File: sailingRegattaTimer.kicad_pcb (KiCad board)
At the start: 2 copper layers, 58 x 68 mm, 29 parts, among them J1 Power, J1-Red-1M1 Conn_01x02_Socket, J2 Digital/PWM, J2-Yel-2M1 Conn_01x02_Socket, J3 Analog, J3-Grn-3M1 J3-Grn-3M, J4 Digital/PWM, J4-Blu-5M1 J4-Blu-5M1, J5-5v-LED1 Conn_01x02_Socket, J6-Reset1 J6-Reset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

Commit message: incremental save
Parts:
- moved D1-LED 0.56 mm to (135.2, 68.6)
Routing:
- net GND: track 165.0 -> 155.5 mm
- net +5V: track 169.1 -> 170.1 mm
- net /4: track 56.0 -> 55.5 mm

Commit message: update files, prep for PCB Way contact
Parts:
- moved D1-LED 0.50 mm to (135.2, 69.1)
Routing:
- net GND: track 155.5 -> 173.5 mm
- net /4: track 55.5 -> 56.0 mm

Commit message: commit to save interim work
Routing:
- net GND: track 173.5 -> 171.3 mm
- net +5V: track 170.1 -> 168.3 mm
- net /4: track 56.0 -> 55.0 mm
- net /2: track 30.2 -> 29.3 mm
- net Net-(D1-K): track 37.0 -> 36.5 mm
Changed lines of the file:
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@@
 	)
 	(segment
-		(start 127 78)
-		(end 127.5 77.5)
+		(start 135 55.25)
+		(end 132 52.25)
 		(width 0.25)
 		(layer "F.Cu")
@@
 	)
 	(segment
-		(start 134.05 60)
-		(end 134 59.95)
-		(width 0.25)
-		(layer "F.Cu")
-		(net 1)
-	)
-	(segment
 		(start 138.75 81.75)
 		(end 138.75 88.75)
@@
 	)
 	(segment
+		(start 135 60.75)
+		(end 135 55.25)
+		(width 0.25)
+		(layer "F.Cu")
+		(net 1)
+	)
+	(segment
 		(start 155.995 92)
 		(end 155.995 94.495)
@@
 	)
 	(segment
-		(start 134 59.95)
-		(end 134 51.75)
+		(start 132 52.25)
+		(end 129.466 52.25)
 		(width 0.25)
 		(layer "F.Cu")
@@
 	)
 	(segment
-		(start 134 51.75)
-		(end 128.966 51.75)
-		(width 0.25)
-		(layer "F.Cu")
-		(net 1)
-	)
-	(segment
 		(start 155.995 70.5)
 		(end 155.995 60.505)
@@
 	)
 	(segment
-		(start 133.3 60.75)
-		(end 134.05 60)
-		(width 0.25)
-		(layer "F.Cu")
-		(net 1)
-	)
-	(segment
-		(start 128.966 51.75)
-		(end 126.416 49.2)
-		(width 0.25)
-		(layer "F.Cu")
-		(net 1)
-	)
-	(segment
-		(start 155.995 60.505)
-		(end 156.5 60)
-		(width 0.25)
-		(layer "F.Cu")
-		(net 1)
-	)
-	(segment
 		(start 145.89 94.75)
 		(end 143.18 97.46)
@@
 	)
 	(segment
+		(start 133.3 60.75)
+		(end 135 60.75)
+		(width 0.25)
+		(layer "F.Cu")
+		(net 1)
+	)
+	(segment
 		(start 155.995 94.495)
 		(end 155.74 94.75)
@@
 	)
 	(segment
-		(start 123.04 88.71)
-		(end 122.5 88.71)
+		(start 129.466 52.25)
+		(end 126.416 49.2)
 		(width 0.25)
 		(layer "F.Cu")
@@
 	)
 	(segment
-		(start 138.25 95.07)
-		(end 140.64 97.46)
+		(start 138.5 94)
+		(end 136 91.5)
+		(width 0.25)
+		(layer "B.Cu")
+		(net 1)
+	)
+	(segment
+		(start 140.64 97.46)
+		(end 140.64 95.14)
+		(width 0.25)
+		(layer "B.Cu")
+		(net 1)
+	)
+	(segment
+		(start 139.5 94)
+		(end 138.5 94)
+		(width 0.25)
+		(layer "B.Cu")
+		(net 1)
+	)
+	(segment
+		(start 140.64 95.14)
+		(end 139.5 94)
 		(width 0.25)
 		(layer "B.Cu")
@@
 	)
 	(segment
-		(start 138.25 91.75)
-		(end 138.25 95.07)
-		(width 0.25)
-		(layer "B.Cu")
-		(net 1)
-	)
-	(segment
 		(start 121.75 68)
 		(end 126.05 68)
@@
 	)
 	(segment
-		(start 136 91.5)
-		(end 138 91.5)
-		(width 0.25)
-		(layer "B.Cu")
-		(net 1)
-	)
-	(segment
 		(start 126.05 68)
 		(end 133.3 60.75)
@@
 	)
 	(segment
-		(start 138 91.5)
-		(end 138.25 91.75)
-		(width 0.25)
-		(layer "B.Cu")
-		(net 1)
-	)
-	(segment
 		(start 133.3 58.55)
 		(end 132.75 58)
@@
 	)
 	(segment
-		(start 142.5 87.5)
-		(end 143 87.5)
-		(width 0.25)
-		(layer "F.Cu")
-		(net 3)
-	)
-	(segment
 		(start 161.79 67.96)
 		(end 162 67.75)
@@
 	)
 	(segment
-		(start 143 87.5)
-		(end 142.75 87.25)
-		(width 0.25)
-		(layer "F.Cu")
-		(net 3)
-	)
-	(segment
 		(start 138 101.25)
 		(end 122.75 101.25)
@@
 	)
 	(segment
-		(start 159.275 87.5)
-		(end 160 88.225)
-		(width 0.25)
-		(layer "B.Cu")
-		(net 3)
-	)
-	(segment
 		(start 149.5 87.5)
 		(end 158 87.5)
@@
 	)
 	(segment
-		(start 160 90.75)
-		(end 160 90.765)
-		(width 0.25)
-		(layer "B.Cu")
-		(net 12)
-	)
-	(segment
 		(start 153.455 92)
 		(end 153.455 89.795)
@@
 	)
 	(segment
-		(start 125.7 60.75)
-		(end 125.7 60.2)
-		(width 0.25)
-		(layer "F.Cu")
-		(net 18)
-	)
-	(segment
 		(start 129.455 60.75)
 		(end 125.7 60.75)
@@
 	)
 	(segment
-		(start 137.77 68.565)
-		(end 137.27 68.565)
-		(width 0.25)
-		(layer "F.Cu")
-		(net 18)
-	)
-	(segment
 		(start 137.77 69.065)
 		(end 137.77 54.43)
@@
 	)
 	(segment
-		(start 153.75 60.25)
-		(end 153.96 60.04)
-		(width 0.25)
-		(layer "F.Cu")
-		(net 19)
-	)
-	(segment
 		(start 158.17 52.25)
 		(end 152.5 52.25)
@@
 	)
 	(segment
-		(start 153.75 60.5)
-		(end 153.75 60.25)
-		(width 0.25)
-		(layer "F.Cu")
-		(net 19)
-	)
-	(segment
 		(start 153.96 60)
 		(end 155.71 58.25)
@@
 	)
 	(segment
-		(start 160 58.25)
-		(end 160.25 58.5)
-		(width 0.25)
-		(layer "F.Cu")
-		(net 19)
-	)
-	(segment
 		(start 145.72 97.46)
 		(end 145.72 100.22)
@@
 	)
 	(segment
-		(start 133.375 81.625)
-		(end 133.02 81.98)
+		(start 133.02 81.98)
+		(end 136.25 78.75)
 		(width 0.25)
 		(layer "F.Cu")
@@
 	)
 	(segment
-		(start 136.5 78.71)
-		(end 136.71 78.71)
-		(width 0.25)
-		(layer "F.Cu")
-		(net 27)
-	)
-	(segment
-		(start 136.25 78.75)
-		(end 133.375 81.625)
-		(width 0.25)
-		(layer "F.Cu")
-		(net 27)
-	)
-	(segment
-		(start 136.71 78.71)
-		(end 136.75 78.75)
-		(width 0.25)
-		(layer "F.Cu")
-		(net 27)
-	)
-	(segment
 		(start 133.02 86.75)
 		(end 133.02 97.46)
@@
 		(width 0.25)
 		(layer "F.Cu")
-		(net 29)
-	)
-	(segment
-		(start 135.23 68.565)
-		(end 135.23 69.065)
-		(width 0.25)
-		(layer "F.Cu")

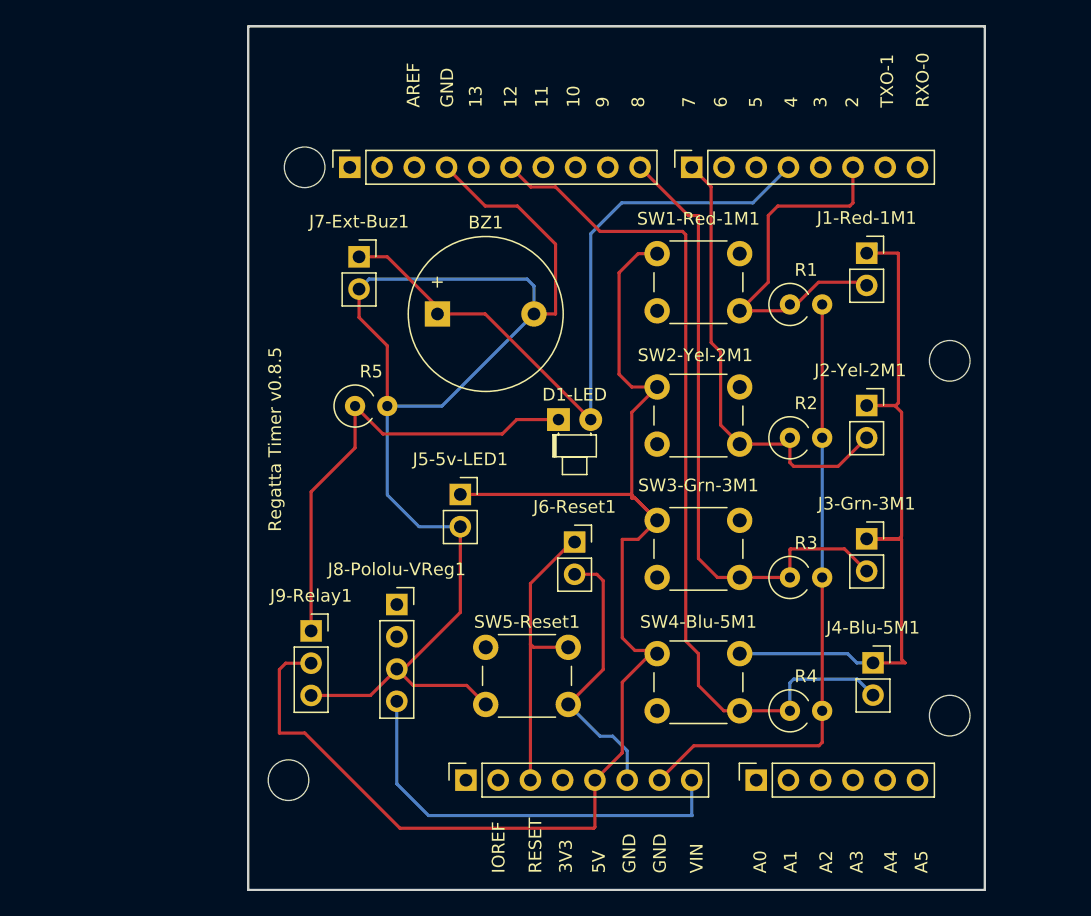
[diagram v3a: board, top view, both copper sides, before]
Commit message: updated board based on physical parts layout
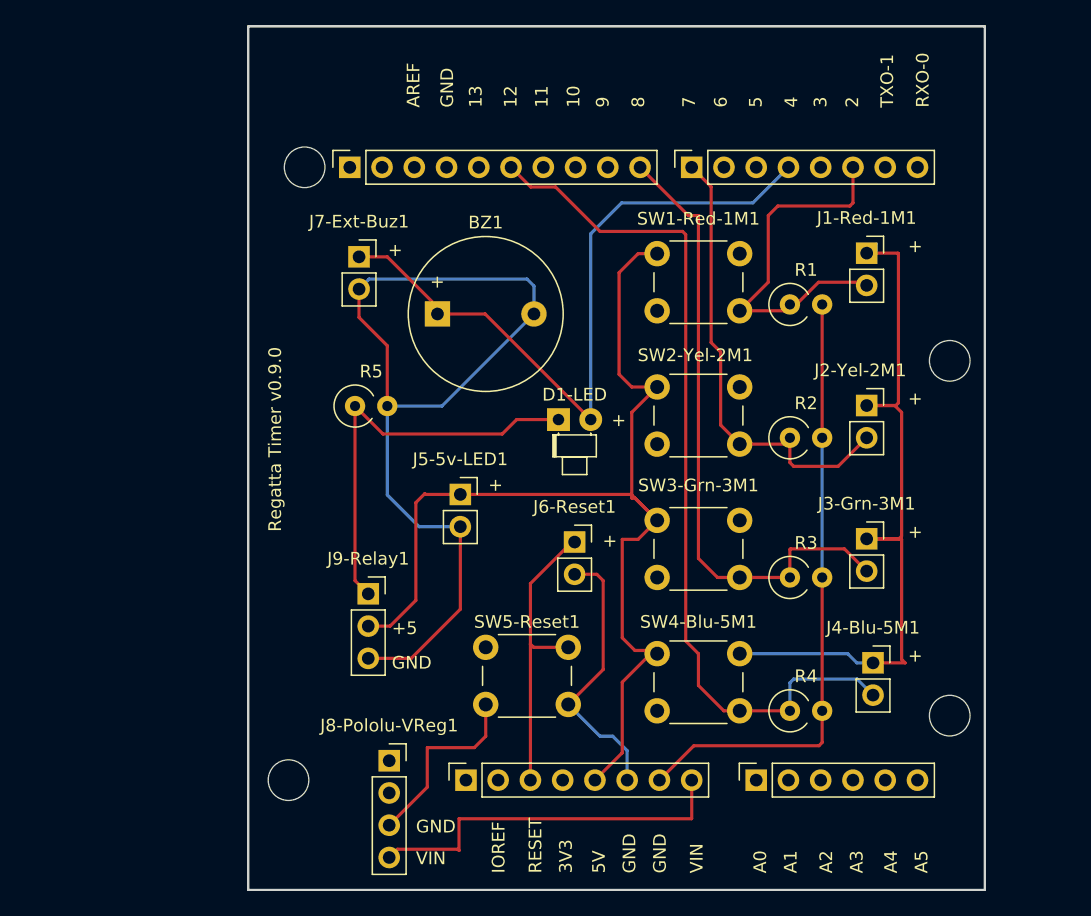
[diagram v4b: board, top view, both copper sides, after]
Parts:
- moved J8-Pololu-VReg1 12.3 mm to (121.9, 95.9)
- moved J9-Relay1 5.36 mm to (120.2, 82.8)
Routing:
- net +5V: track 168.3 -> 145.0 mm
- net GND: track 171.3 -> 155.0 mm
- net VCC: track 33.6 -> 29.7 mm
- net Net-(D1-K): track 36.5 -> 32.6 mm
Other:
- board text added: "+"
- board text added: "+5"
- board text added: "Regatta Timer v0.9.0"
- board text removed: "Regatta Timer v0.8.5"

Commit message: save today's work
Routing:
- net GND: track 155.0 -> 149.2 mm
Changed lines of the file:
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@@
+	)
+	(segment
+		(start 123.88 91.5)
+		(end 129.5 91.5)
+		(width 0.25)
+		(layer "F.Cu")
+		(net 1)
 	)
 	(segment
@@
 		(start 155.995 92)
 		(end 155.995 94.495)
+		(width 0.25)
+		(layer "F.Cu")
+		(net 1)
+	)
+	(segment
+		(start 120.25 87.87)
+		(end 123.88 91.5)
 		(width 0.25)
 		(layer "F.Cu")
@@
 	)
 	(segment
-		(start 120.315 58)
-		(end 119.525 58.79)
-		(width 0.25)
-		(layer "B.Cu")
-		(net 1)
-	)
-	(segment
 		(start 126.05 68)
 		(end 133.3 60.75)
-		(width 0.25)
-		(layer "B.Cu")
-		(net 1)
-	)
-	(segment
-		(start 132.75 58)
-		(end 120.315 58)
-		(width 0.25)
-		(layer "B.Cu")
-		(net 1)
-	)
-	(segment
-		(start 133.3 60.75)
-		(end 133.3 58.55)
 		(width 0.25)
 		(layer "B.Cu")
@@
 		(width 0.25)
 		(layer "B.Cu")
-		(net 1)
-	)
-	(segment
-		(start 133.3 58.55)
-		(end 132.75 58)
-		(width 0.25)
-		(layer "B.Cu")

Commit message: save current working files
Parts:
- removed J1-Red-1M1, J2-Yel-2M1: Conn_01x02_Socket, Connector_PinSocket_2.54mm:PinSocket_1x02_P2.54mm_Vertical
- removed J3-Grn-3M1: J3-Grn-3M, Connector_PinSocket_2.54mm:PinSocket_1x02_P2.54mm_Vertical
- removed J4-Blu-5M1: J4-Blu-5M1, Connector_PinSocket_2.54mm:PinSocket_1x02_P2.54mm_Vertical
- added D1-LED1: LED, LED_THT:LED_D1.8mm_W1.8mm_H2.4mm_Horizontal_O1.27mm_Z1.6mm, F.Cu at (96.4, 82.9)
- added J10-12v-In1: Conn_01x02_Socket, Connector_PinSocket_2.54mm:PinSocket_1x02_P2.54mm_Vertical, F.Cu at (99.1, 60.5)
- added J5: Timers, Connector_PinSocket_2.54mm:PinSocket_1x08_P2.54mm_Vertical, F.Cu at (164.2, 68.8)
- moved R4 35.3 mm to (156.5, 56.8)
- moved SW1-Red-1M1 31.3 mm to (145.5, 87.2)
- moved SW4-Blu-5M1 31.2 mm to (145.6, 56.5)
- moved R1 27.7 mm to (156.0, 87.5)
- moved R3 14.2 mm to (155.9, 67.5)
- moved SW2-Yel-2M1 11.0 mm to (145.6, 77.2)
- moved SW3-Grn-3M1 10.2 mm to (145.4, 67.2)
- moved R2 7.54 mm to (156.0, 77.6)
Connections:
- BZ1 pad 1: /4 -> Net-(BZ1-+)
- BZ1 pad 2: GND -> Net-(BZ1--)
- J5-5v-LED1 pad 1: +5V -> Net-(J5-5v-LED1-Pin_1)
- J5-5v-LED1 pad 2: GND -> Net-(BZ1--)
- J6-Reset1 pad 1: /~{RESET} -> Net-(J6-Reset1-Pin_1)
- J6-Reset1 pad 2: GND -> Net-(BZ1--)
- J7-Ext-Buz1 pad 1: /4 -> Net-(BZ1-+)
- J7-Ext-Buz1 pad 2: GND -> Net-(BZ1--)
- J8-Pololu-VReg1 pad 2: unconnected-(J8-Pololu-VReg1-Pin_2-Pad2) -> Net-(J10-12v-In1-Pin_1)
- J8-Pololu-VReg1 pad 3: GND -> Net-(BZ1--)
- J8-Pololu-VReg1 pad 4: VCC -> Net-(J8-Pololu-VReg1-Pin_4)
- J9-Relay1 pad 1: Net-(D1-K) -> Net-(BZ1-+)
- J9-Relay1 pad 2: +5V -> Net-(J5-5v-LED1-Pin_1)
- J9-Relay1 pad 3: GND -> Net-(BZ1--)
- R1 pad 1: /2 -> Net-(J5-Pin_8)
- R1 pad 2: GND -> Net-(BZ1--)
- R2 pad 1: /7 -> Net-(J5-Pin_6)
- R2 pad 2: GND -> Net-(BZ1--)
- R3 pad 1: /8 -> Net-(J5-Pin_4)
- R3 pad 2: GND -> Net-(BZ1--)
- R4 pad 1: /12 -> Net-(J5-Pin_2)
- R4 pad 2: GND -> Net-(BZ1--)
- R5 pad 1: Net-(D1-K) -> Net-(D1-LED1-K)
- R5 pad 2: GND -> Net-(BZ1--)
- SW1-Red-1M1 pad 1: +5V -> Net-(J5-5v-LED1-Pin_1)
- SW1-Red-1M1 pad 2: /2 -> Net-(J5-Pin_8)
- SW2-Yel-2M1 pad 1: +5V -> Net-(J5-5v-LED1-Pin_1)
- SW2-Yel-2M1 pad 2: /7 -> Net-(J5-Pin_6)
- SW3-Grn-3M1 pad 1: +5V -> Net-(J5-5v-LED1-Pin_1)
- SW3-Grn-3M1 pad 2: /8 -> Net-(J5-Pin_4)
- SW4-Blu-5M1 pad 1: +5V -> Net-(J5-5v-LED1-Pin_1)
- SW4-Blu-5M1 pad 2: /12 -> Net-(J5-Pin_2)
- SW5-Reset1 pad 1: /~{RESET} -> Net-(J6-Reset1-Pin_1)
- SW5-Reset1 pad 2: GND -> Net-(BZ1--)
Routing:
- net Net-(BZ1--): track 0.00 -> 149.3 mm
- net +5V: track 145.0 -> 0.00 mm
- net GND: track 149.2 -> 21.8 mm
- net Net-(J5-5v-LED1-Pin_1): track 0.00 -> 89.0 mm
- net /12: track 69.3 -> 0.00 mm
- net /8: track 50.0 -> 0.00 mm
- net /7: track 36.4 -> 0.00 mm
- net /2: track 29.3 -> 0.00 mm
- net Net-(J5-Pin_2): track 0.00 -> 12.6 mm
- net Net-(J5-Pin_8): track 0.00 -> 12.3 mm
- net Net-(J5-Pin_4): track 0.00 -> 12.3 mm
- net Net-(J5-Pin_6): track 0.00 -> 12.3 mm
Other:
- board text added: "1M Blue Purple"
- board text added: "2M Green Orange"
- board text added: "3M White Yellow"
- board text added: "5M Black Red"
